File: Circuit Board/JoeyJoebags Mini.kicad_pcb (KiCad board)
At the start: 2 copper layers, 50 x 29.2 mm, 2 parts

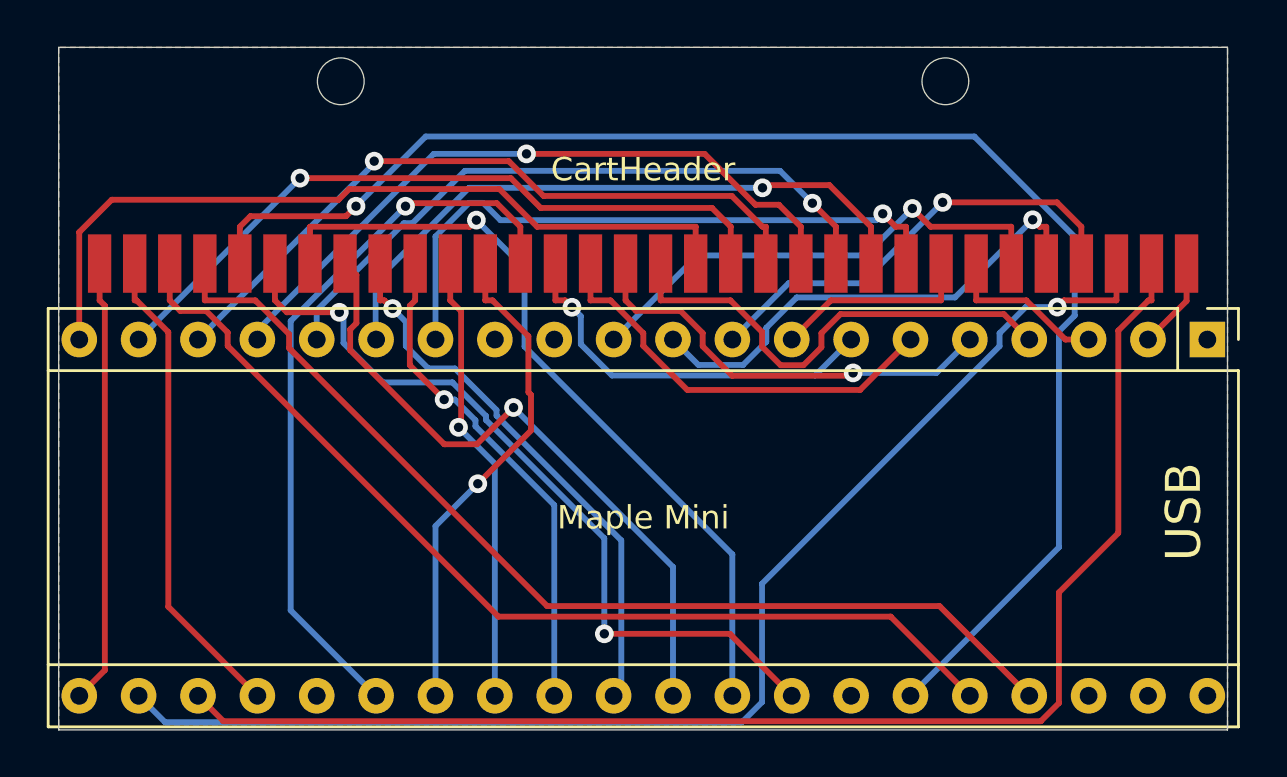
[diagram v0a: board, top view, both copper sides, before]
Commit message: Fix broken footprint for maple mini
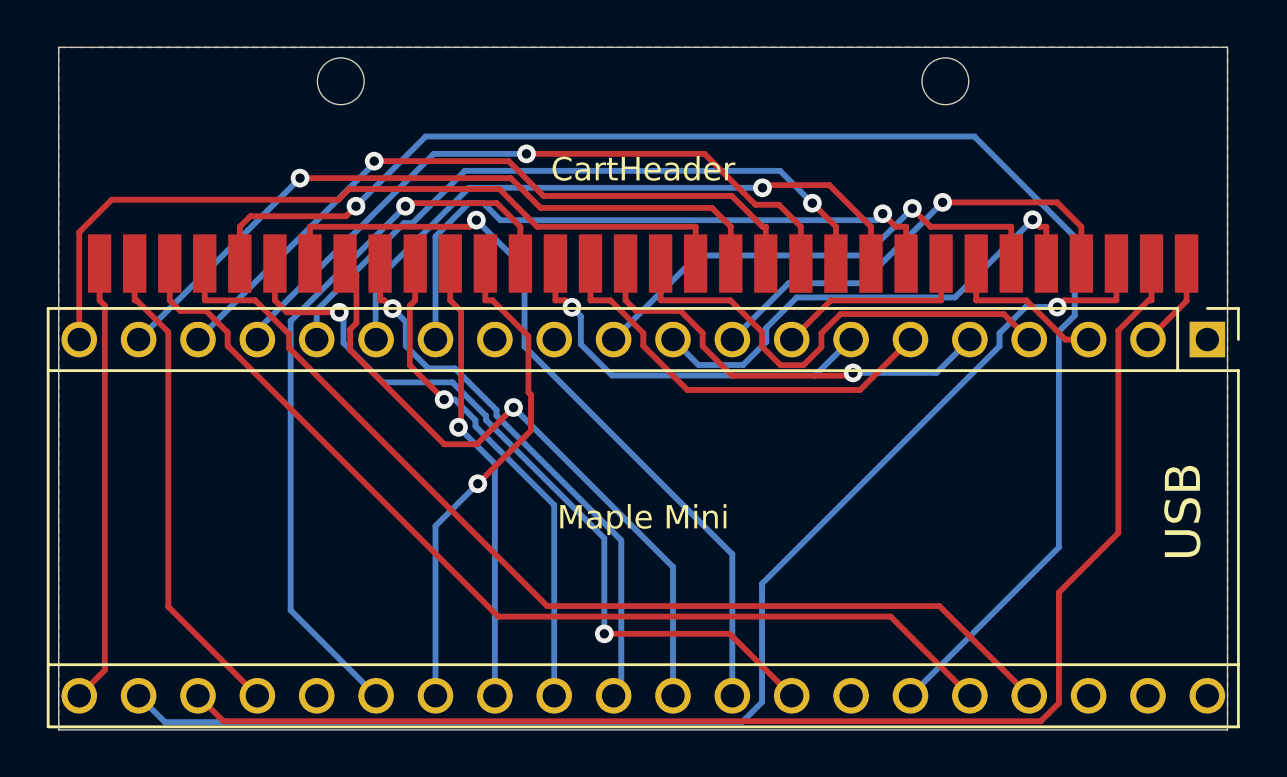
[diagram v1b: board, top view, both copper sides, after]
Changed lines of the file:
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@@
       (effects (font (size 1 1) (thickness 0.15)))
     )
-    (fp_text value Maple_Mini (at 7.62 26.035 90) (layer F.Fab)
+    (fp_text value Maple_Mini (at 7.62 26.035 270) (layer F.Fab)
       (effects (font (size 1 1) (thickness 0.15)))
     )
@@
     (fp_line (start -1.27 -0.635) (end -0.635 -1.27) (layer F.Fab) (width 0.1))
     (fp_line (start 13.97 -1.27) (end 13.97 49.53) (layer F.Fab) (width 0.1))
-    (fp_text user %R (at 7.62 24.13 90) (layer F.Fab)
+    (fp_text user %R (at 7.62 24.13 270) (layer F.Fab)
       (effects (font (size 1 1) (thickness 0.15)))
     )
     (fp_line (start 3.81 6.604) (end 11.43 6.604) (layer F.Fab) (width 0.1))
-    (pad 1 thru_hole rect (at 0 0 270) (size 1.524 1.524) (drill 0.762) (layers *.Cu *.Mask)
+    (pad 1 thru_hole rect (at 0 0 270) (size 1.524 1.524) (drill 1) (layers *.Cu *.Mask)
       (net 1 "Net-(A1-Pad1)"))
-    (pad 2 thru_hole circle (at 0 2.54 270) (size 1.524 1.524) (drill 0.762) (layers *.Cu *.Mask)
+    (pad 2 thru_hole circle (at 0 2.54 270) (size 1.524 1.524) (drill 1) (layers *.Cu *.Mask)
       (net 2 GND))
-    (pad 3 thru_hole circle (at 0 5.08 270) (size 1.524 1.524) (drill 0.762) (layers *.Cu *.Mask)
+    (pad 3 thru_hole circle (at 0 5.08 270) (size 1.524 1.524) (drill 1) (layers *.Cu *.Mask)
       (net 3 D32-boot0))
-    (pad 4 thru_hole circle (at 0 7.62 270) (size 1.524 1.524) (drill 0.762) (layers *.Cu *.Mask)
+    (pad 4 thru_hole circle (at 0 7.62 270) (size 1.524 1.524) (drill 1) (layers *.Cu *.Mask)
       (net 4 M15))
-    (pad 5 thru_hole circle (at 0 10.16 270) (size 1.524 1.524) (drill 0.762) (layers *.Cu *.Mask)
+    (pad 5 thru_hole circle (at 0 10.16 270) (size 1.524 1.524) (drill 1) (layers *.Cu *.Mask)
       (net 5 M16))
-    (pad 6 thru_hole circle (at 0 12.7 270) (size 1.524 1.524) (drill 0.762) (layers *.Cu *.Mask)
+    (pad 6 thru_hole circle (at 0 12.7 270) (size 1.524 1.524) (drill 1) (layers *.Cu *.Mask)
       (net 6 M17))
-    (pad 7 thru_hole circle (at 0 15.24 270) (size 1.524 1.524) (drill 0.762) (layers *.Cu *.Mask)
+    (pad 7 thru_hole circle (at 0 15.24 270) (size 1.524 1.524) (drill 1) (layers *.Cu *.Mask)
       (net 7 M18))
-    (pad 8 thru_hole circle (at 0 17.78 270) (size 1.524 1.524) (drill 0.762) (layers *.Cu *.Mask)
+    (pad 8 thru_hole circle (at 0 17.78 270) (size 1.524 1.524) (drill 1) (layers *.Cu *.Mask)
       (net 8 M19))
-    (pad 9 thru_hole circle (at 0 20.32 270) (size 1.524 1.524) (drill 0.762) (layers *.Cu *.Mask)
+    (pad 9 thru_hole circle (at 0 20.32 270) (size 1.524 1.524) (drill 1) (layers *.Cu *.Mask)
       (net 9 M20))
-    (pad 10 thru_hole circle (at 0 22.86 270) (size 1.524 1.524) (drill 0.762) (layers *.Cu *.Mask)
+    (pad 10 thru_hole circle (at 0 22.86 270) (size 1.524 1.524) (drill 1) (layers *.Cu *.Mask)
       (net 10 M21))
-    (pad 11 thru_hole circle (at 0 25.4 270) (size 1.524 1.524) (drill 0.762) (layers *.Cu *.Mask)
+    (pad 11 thru_hole circle (at 0 25.4 270) (size 1.524 1.524) (drill 1) (layers *.Cu *.Mask)
       (net 11 M22))
-    (pad 12 thru_hole circle (at 0 27.94 270) (size 1.524 1.524) (drill 0.762) (layers *.Cu *.Mask)
+    (pad 12 thru_hole circle (at 0 27.94 270) (size 1.524 1.524) (drill 1) (layers *.Cu *.Mask)
       (net 12 "Net-(A1-Pad12)"))
-    (pad 13 thru_hole circle (at 0 30.48 270) (size 1.524 1.524) (drill 0.762) (layers *.Cu *.Mask)
+    (pad 13 thru_hole circle (at 0 30.48 270) (size 1.524 1.524) (drill 1) (layers *.Cu *.Mask)
       (net 13 "Net-(A1-Pad13)"))
-    (pad 14 thru_hole circle (at 0 33.02 270) (size 1.524 1.524) (drill 0.762) (layers *.Cu *.Mask)
+    (pad 14 thru_hole circle (at 0 33.02 270) (size 1.524 1.524) (drill 1) (layers *.Cu *.Mask)
       (net 14 M25))
-    (pad 15 thru_hole circle (at 0 35.56 270) (size 1.524 1.524) (drill 0.762) (layers *.Cu *.Mask)
+    (pad 15 thru_hole circle (at 0 35.56 270) (size 1.524 1.524) (drill 1) (layers *.Cu *.Mask)
       (net 15 M26))
-    (pad 16 thru_hole circle (at 0 38.1 270) (size 1.524 1.524) (drill 0.762) (layers *.Cu *.Mask)
+    (pad 16 thru_hole circle (at 0 38.1 270) (size 1.524 1.524) (drill 1) (layers *.Cu *.Mask)
       (net 16 M27))
-    (pad 17 thru_hole circle (at 0 40.64 270) (size 1.524 1.524) (drill 0.762) (layers *.Cu *.Mask)
+    (pad 17 thru_hole circle (at 0 40.64 270) (size 1.524 1.524) (drill 1) (layers *.Cu *.Mask)
       (net 17 M28))
-    (pad 18 thru_hole circle (at 0 43.18 270) (size 1.524 1.524) (drill 0.762) (layers *.Cu *.Mask)
+    (pad 18 thru_hole circle (at 0 43.18 270) (size 1.524 1.524) (drill 1) (layers *.Cu *.Mask)
       (net 18 M29))
-    (pad 19 thru_hole circle (at 0 45.72 270) (size 1.524 1.524) (drill 0.762) (layers *.Cu *.Mask)
+    (pad 19 thru_hole circle (at 0 45.72 270) (size 1.524 1.524) (drill 1) (layers *.Cu *.Mask)
       (net 19 M30))
-    (pad 20 thru_hole circle (at 0 48.26 270) (size 1.524 1.524) (drill 0.762) (layers *.Cu *.Mask)
+    (pad 20 thru_hole circle (at 0 48.26 270) (size 1.524 1.524) (drill 1) (layers *.Cu *.Mask)
       (net 20 M31))
-    (pad 21 thru_hole circle (at 15.24 48.26 270) (size 1.524 1.524) (drill 0.762) (layers *.Cu *.Mask)
+    (pad 21 thru_hole circle (at 15.24 48.26 270) (size 1.524 1.524) (drill 1) (layers *.Cu *.Mask)
       (net 21 VIN))
-    (pad 22 thru_hole circle (at 15.24 45.72 270) (size 1.524 1.524) (drill 0.762) (layers *.Cu *.Mask)
+    (pad 22 thru_hole circle (at 15.24 45.72 270) (size 1.524 1.524) (drill 1) (layers *.Cu *.Mask)
       (net 22 M0))
-    (pad 23 thru_hole circle (at 15.24 43.18 270) (size 1.524 1.524) (drill 0.762) (layers *.Cu *.Mask)
+    (pad 23 thru_hole circle (at 15.24 43.18 270) (size 1.524 1.524) (drill 1) (layers *.Cu *.Mask)
       (net 23 M1))
-    (pad 24 thru_hole circle (at 15.24 40.64 270) (size 1.524 1.524) (drill 0.762) (layers *.Cu *.Mask)
+    (pad 24 thru_hole circle (at 15.24 40.64 270) (size 1.524 1.524) (drill 1) (layers *.Cu *.Mask)
       (net 24 D2-boot1))
-    (pad 25 thru_hole circle (at 15.24 38.1 270) (size 1.524 1.524) (drill 0.762) (layers *.Cu *.Mask)
+    (pad 25 thru_hole circle (at 15.24 38.1 270) (size 1.524 1.524) (drill 1) (layers *.Cu *.Mask)
       (net 25 "Net-(A1-Pad25)"))
-    (pad 26 thru_hole circle (at 15.24 35.56 270) (size 1.524 1.524) (drill 0.762) (layers *.Cu *.Mask)
+    (pad 26 thru_hole circle (at 15.24 35.56 270) (size 1.524 1.524) (drill 1) (layers *.Cu *.Mask)
       (net 26 M4))
-    (pad 27 thru_hole circle (at 15.24 33.02 270) (size 1.524 1.524) (drill 0.762) (layers *.Cu *.Mask)
+    (pad 27 thru_hole circle (at 15.24 33.02 270) (size 1.524 1.524) (drill 1) (layers *.Cu *.Mask)
       (net 27 M5))
-    (pad 28 thru_hole circle (at 15.24 30.48 270) (size 1.524 1.524) (drill 0.762) (layers *.Cu *.Mask)
+    (pad 28 thru_hole circle (at 15.24 30.48 270) (size 1.524 1.524) (drill 1) (layers *.Cu *.Mask)
       (net 28 M6))
-    (pad 29 thru_hole circle (at 15.24 27.94 270) (size 1.524 1.524) (drill 0.762) (layers *.Cu *.Mask)
+    (pad 29 thru_hole circle (at 15.24 27.94 270) (size 1.524 1.524) (drill 1) (layers *.Cu *.Mask)
       (net 29 M7))
-    (pad 30 thru_hole circle (at 15.24 25.4 270) (size 1.524 1.524) (drill 0.762) (layers *.Cu *.Mask)
+    (pad 30 thru_hole circle (at 15.24 25.4 270) (size 1.524 1.524) (drill 1) (layers *.Cu *.Mask)
       (net 30 M8))
-    (pad 31 thru_hole circle (at 15.24 22.86 270) (size 1.524 1.524) (drill 0.762) (layers *.Cu *.Mask)
+    (pad 31 thru_hole circle (at 15.24 22.86 270) (size 1.524 1.524) (drill 1) (layers *.Cu *.Mask)
       (net 31 M9))
-    (pad 32 thru_hole circle (at 15.24 20.32 270) (size 1.524 1.524) (drill 0.762) (layers *.Cu *.Mask)
+    (pad 32 thru_hole circle (at 15.24 20.32 270) (size 1.524 1.524) (drill 1) (layers *.Cu *.Mask)
       (net 32 M10))
-    (pad 33 thru_hole circle (at 15.24 17.78 270) (size 1.524 1.524) (drill 0.762) (layers *.Cu *.Mask)
+    (pad 33 thru_hole circle (at 15.24 17.78 270) (size 1.524 1.524) (drill 1) (layers *.Cu *.Mask)
       (net 33 M11))
-    (pad 34 thru_hole circle (at 15.24 15.24 270) (size 1.524 1.524) (drill 0.762) (layers *.Cu *.Mask)
+    (pad 34 thru_hole circle (at 15.24 15.24 270) (size 1.524 1.524) (drill 1) (layers *.Cu *.Mask)
       (net 34 "Net-(A1-Pad34)"))
-    (pad 35 thru_hole circle (at 15.24 12.7 270) (size 1.524 1.524) (drill 0.762) (layers *.Cu *.Mask)
+    (pad 35 thru_hole circle (at 15.24 12.7 270) (size 1.524 1.524) (drill 1) (layers *.Cu *.Mask)
       (net 35 M12))
-    (pad 36 thru_hole circle (at 15.24 10.16 270) (size 1.524 1.524) (drill 0.762) (layers *.Cu *.Mask)
+    (pad 36 thru_hole circle (at 15.24 10.16 270) (size 1.524 1.524) (drill 1) (layers *.Cu *.Mask)
       (net 36 M13))
-    (pad 37 thru_hole circle (at 15.24 7.62 270) (size 1.524 1.524) (drill 0.762) (layers *.Cu *.Mask)
+    (pad 37 thru_hole circle (at 15.24 7.62 270) (size 1.524 1.524) (drill 1) (layers *.Cu *.Mask)
       (net 37 M14))
-    (pad 38 thru_hole circle (at 15.24 5.08 270) (size 1.524 1.524) (drill 0.762) (layers *.Cu *.Mask)
+    (pad 38 thru_hole circle (at 15.24 5.08 270) (size 1.524 1.524) (drill 1) (layers *.Cu *.Mask)
       (net 38 "Net-(A1-Pad38)"))
-    (pad 39 thru_hole circle (at 15.24 2.54 270) (size 1.524 1.524) (drill 0.762) (layers *.Cu *.Mask)
+    (pad 39 thru_hole circle (at 15.24 2.54 270) (size 1.524 1.524) (drill 1) (layers *.Cu *.Mask)
       (net 39 "Net-(A1-Pad39)"))
-    (pad 40 thru_hole circle (at 15.24 0 270) (size 1.524 1.524) (drill 0.762) (layers *.Cu *.Mask)
+    (pad 40 thru_hole circle (at 15.24 0 270) (size 1.524 1.524) (drill 1) (layers *.Cu *.Mask)
       (net 40 "Net-(A1-Pad40)"))
     (model ${KISYS3DMOD}/Module.3dshapes/Maple_Mini.wrl
